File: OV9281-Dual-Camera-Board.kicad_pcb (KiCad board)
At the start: 4 copper layers, 100 x 25 mm, 83 parts, among them IC1 TLV73328PDBVT, IC2 TLV73318PDBVT, IC3 TLV73312PDBVT, J3 WE_68715014522, Q1 BSS138AKA, U1 OV9281, U2 OV9281, U3 NTS0104BQ, U4 NTB0104BQ, Y1 Farnell_1842027, Y2 Farnell_1842027

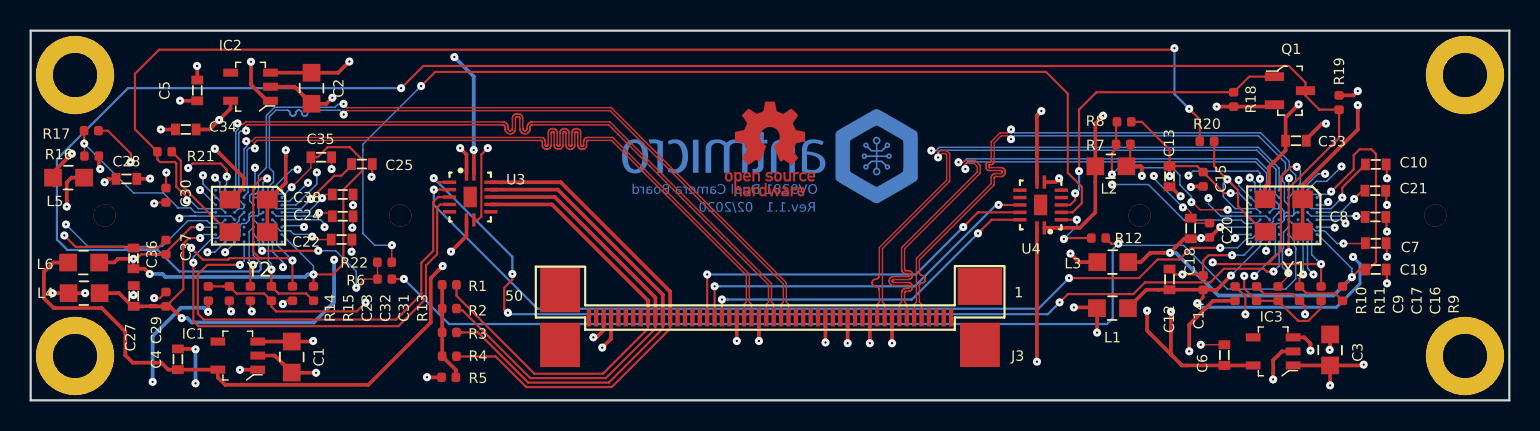
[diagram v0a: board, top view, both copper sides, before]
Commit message: Improve camera lenses
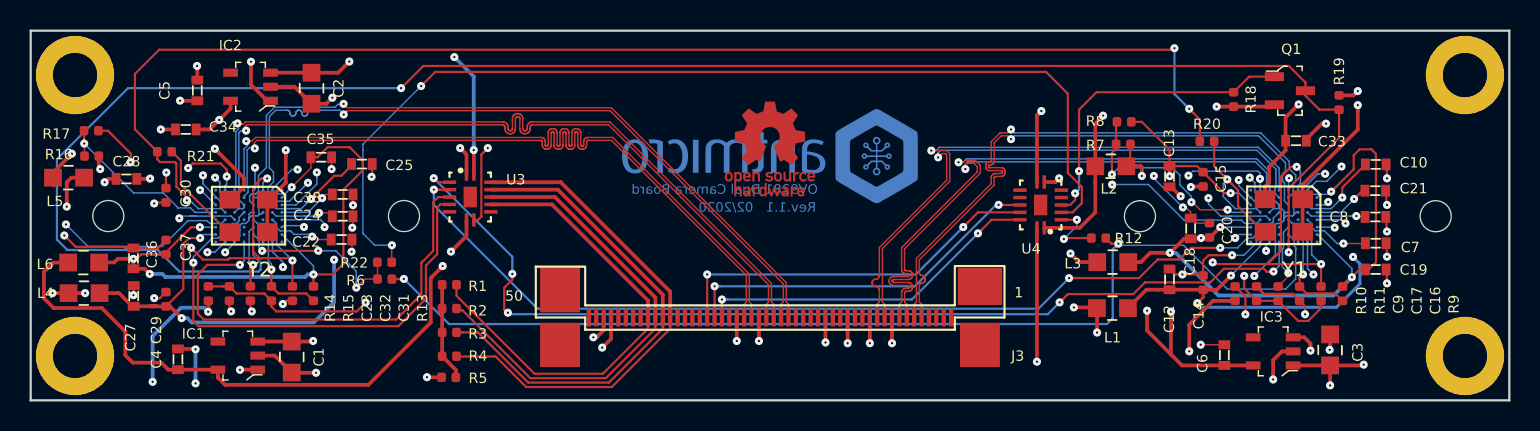
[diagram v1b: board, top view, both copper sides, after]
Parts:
- MP5, MP6: footprint OV9281-Dual-Camera-Board-footprints:Camera_Lens_20mm -> antmicro-footprints:Camera_Lens_20mm_ARDUCAM_M27280M07S
- Y1, Y2: value Farnell_1842027 -> 7C-24.000MBB-T
- moved MP5 10.2 mm to (125.2, 112.5)
- moved MP6 10.0 mm to (195.0, 112.5)
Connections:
- J3 pad 1: Net-(J3-Pad1) -> unconnected-(J3-Pad1)
- J3 pad 13: Net-(J3-Pad13) -> unconnected-(J3-Pad13)
- J3 pad 14: Net-(J3-Pad14) -> unconnected-(J3-Pad14)
- J3 pad 16: Net-(J3-Pad16) -> unconnected-(J3-Pad16)
- J3 pad 17: Net-(J3-Pad17) -> unconnected-(J3-Pad17)
- J3 pad 19: Net-(J3-Pad19) -> unconnected-(J3-Pad19)
- J3 pad 2: Net-(J3-Pad2) -> unconnected-(J3-Pad2)
- J3 pad 20: Net-(J3-Pad20) -> unconnected-(J3-Pad20)
- J3 pad 21: Net-(J3-Pad21) -> unconnected-(J3-Pad21)
- J3 pad 22: Net-(J3-Pad22) -> unconnected-(J3-Pad22)
- J3 pad 3: Net-(J3-Pad3) -> unconnected-(J3-Pad3)
- J3 pad 31: Net-(J3-Pad31) -> unconnected-(J3-Pad31)
- J3 pad 35: Net-(J3-Pad35) -> unconnected-(J3-Pad35)
- J3 pad 36: Net-(J3-Pad36) -> unconnected-(J3-Pad36)
- J3 pad 37: Net-(J3-Pad37) -> unconnected-(J3-Pad37)
- J3 pad 38: Net-(J3-Pad38) -> unconnected-(J3-Pad38)
- J3 pad 4: Net-(J3-Pad4) -> unconnected-(J3-Pad4)
- J3 pad 43: Net-(J3-Pad43) -> unconnected-(J3-Pad43)
- J3 pad 44: Net-(J3-Pad44) -> unconnected-(J3-Pad44)
- J3 pad 45: Net-(J3-Pad45) -> unconnected-(J3-Pad45)
- J3 pad 46: Net-(J3-Pad46) -> unconnected-(J3-Pad46)
- J3 pad 49: Net-(J3-Pad49) -> unconnected-(J3-Pad49)
- J3 pad 50: Net-(J3-Pad50) -> unconnected-(J3-Pad50)
- U1 pad A6: Net-(U1-PadA6) -> unconnected-(U1-PadA6)
- U1 pad B4: Net-(U1-PadB4) -> unconnected-(U1-PadB4)
- U1 pad B6: Net-(U1-PadB6) -> unconnected-(U1-PadB6)
- U1 pad C2: Net-(U1-PadC2) -> unconnected-(U1-PadC2)
- U1 pad C3: Net-(U1-PadC3) -> unconnected-(U1-PadC3)
- U1 pad C4: Net-(U1-PadC4) -> unconnected-(U1-PadC4)
- U1 pad C6: Net-(U1-PadC6) -> unconnected-(U1-PadC6)
- U1 pad C7: Net-(U1-PadC7) -> unconnected-(U1-PadC7)
- U1 pad D1: Net-(U1-PadD1) -> unconnected-(U1-PadD1)
- U1 pad D4: Net-(U1-PadD4) -> unconnected-(U1-PadD4)
- U1 pad D6: Net-(U1-PadD6) -> unconnected-(U1-PadD6)
- U2 pad A6: Net-(U2-PadA6) -> unconnected-(U2-PadA6)
- U2 pad B4: Net-(U2-PadB4) -> unconnected-(U2-PadB4)
- U2 pad B6: Net-(U2-PadB6) -> unconnected-(U2-PadB6)
- U2 pad C2: Net-(U2-PadC2) -> unconnected-(U2-PadC2)
- U2 pad C3: Net-(U2-PadC3) -> unconnected-(U2-PadC3)
- U2 pad C4: Net-(U2-PadC4) -> unconnected-(U2-PadC4)
- U2 pad C6: Net-(U2-PadC6) -> unconnected-(U2-PadC6)
- U2 pad C7: Net-(U2-PadC7) -> unconnected-(U2-PadC7)
- U2 pad D1: Net-(U2-PadD1) -> unconnected-(U2-PadD1)
- U2 pad D4: Net-(U2-PadD4) -> unconnected-(U2-PadD4)
- U2 pad D6: Net-(U2-PadD6) -> unconnected-(U2-PadD6)
- U3 pad 6: Net-(U3-Pad6) -> unconnected-(U3-Pad6)
- U3 pad 9: Net-(U3-Pad9) -> unconnected-(U3-Pad9)
- U4 pad 10: Net-(U4-Pad10) -> unconnected-(U4-Pad10)
- U4 pad 5: Net-(U4-Pad5) -> unconnected-(U4-Pad5)
- U4 pad 6: Net-(U4-Pad6) -> unconnected-(U4-Pad6)
- U4 pad 9: Net-(U4-Pad9) -> unconnected-(U4-Pad9)
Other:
- net class Default removed
- net class Supply removed
